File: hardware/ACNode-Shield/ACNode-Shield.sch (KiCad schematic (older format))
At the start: 8 parts

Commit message: PCB rev 1
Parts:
- removed CON?: SD_Card, 10067847-001, symbol SD_Card
- added C1: 10nF, Capacitors_SMD:C_1210_HandSoldering, symbol C_Small
- added D1: 1N4007, Diodes_ThroughHole:Diode_DO-41_SOD81_Horizontal_RM10, symbol D
- added J1: MICRO_SD_HINGE, armory:MICRO_SD_HINGE_AMP, symbol MICRO_SD_HINGE
- added P2: CONN_RELAY, Pin_Headers:Pin_Header_Straight_1x03, symbol CONN_01X03
- added Q1: PN2222A, TO_SOT_Packages_THT:TO-92_Inline_Wide, symbol PN2222A
- added R1: 10k, Resistors_ThroughHole:Resistor_Horizontal_RM10mm, symbol R
- added R2: 100, Resistors_ThroughHole:Resistor_Horizontal_RM10mm, symbol R
- added SW2: SW_BTN, Socket_Strips:Socket_Strip_Straight_1x02, symbol SW_PUSH
- added U1: SRD-05VDC-SL-C, Relays_ThroughHole:Relay_SANYOU_SRD_Series_Form_C, symbol SRD-05VDC-SL-C
- P1, P3: renamed from P?; footprint (none) -> Pin_Headers:Pin_Header_Straight_1x04
- P4, P5: renamed from P?; footprint (none) -> Socket_Strips:Socket_Strip_Straight_2x10
- P6: renamed from P?; footprint (none) -> Pin_Headers:Pin_Header_Straight_1x03
- SW1: renamed from SW?; footprint (none) -> Buttons_Switches_ThroughHole:SW_PUSH_SMALL
- U2: renamed from U?; footprint (none) -> ws2812:WS2812b
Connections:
- net PQ2/PA3 is gone; now on net PQ2: P5.12 (P12)
- net PQ3/PA2 is gone; now on net PQ3: P5.14 (P14)
- net +3.3v: now also C1.2, J1.5 (CLK)
- net +5V: now also D1.1 (K), U1.5 (RL)
- net GND: now also C1.1, J1.3 (CMD), R2.2, SW2.2
- net PB4: no longer U2.4 (DIN)
- net PG1: now also R1.2
- net PM7: now also SW2.1
- net PP5: now also U2.4 (DIN)
- net PQ0: now also J1.4 (VDD)
- net PQ1: now also J1.7 (DAT0)
- net PQ2: now also J1.2 (DAT3/CD)
- net PQ3: now also J1.6 (VSS/GND)
- new net: P2.2 (P2), U1.1 (COM)
- new net: D1.2 (A), Q1.3 (C), U1.2 (RL)
- new net: P2.3 (P3), U1.3 (NC)
- new net: P2.1 (P1), U1.4 (NO)
- new net: Q1.1 (E), R2.1
- new net: Q1.2 (B), R1.1
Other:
- moved on the sheet: P4, P5

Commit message: Removed a resistor, fixed some tracks.
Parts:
- removed R2: 100, Resistors_ThroughHole:Resistor_Horizontal_RM10mm, symbol R
- R1: value 10k -> 1k
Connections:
- net GND: now also Q1.1 (E)
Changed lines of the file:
@@
 +5V
-$Comp
-L R R2
-U 1 1 572DD805
-P 2750 3050
-F 0 "R2" H 2820 3096 50  0000 L CNN
-F 1 "100" H 2820 3004 50  0000 L CNN
-F 2 "Resistors_ThroughHole:Resistor_Horizontal_RM10mm" V 2680 3050 50  0001 C CNN
-F 3 "" H 2750 3050 50  0000 C CNN
-	1    2750 3050
-	1    0    0    -1
-$EndComp
 $Comp
 L D D1
@@
 Connection ~ 2750 1850
 Wire Wire Line
-	2750 2800 2750 2900
+	2750 2800 2750 3300
 Text GLabel 2100 3300 0    60   Input ~ 0
 GND
 Wire Wire Line
-	2100 3300 2750 3300
-Wire Wire Line
-	2750 3300 2750 3200
+	2750 3300 2100 3300
 $Comp
 L R R1
@@
 P 2200 2600
 F 0 "R1" V 1992 2600 50  0000 C CNN
-F 1 "10k" V 2084 2600 50  0000 C CNN
+F 1 "1k" V 2084 2600 50  0000 C CNN
 F 2 "Resistors_ThroughHole:Resistor_Horizontal_RM10mm" V 2130 2600 50  0001 C CNN
 F 3 "" H 2200 2600 50  0000 C CNN

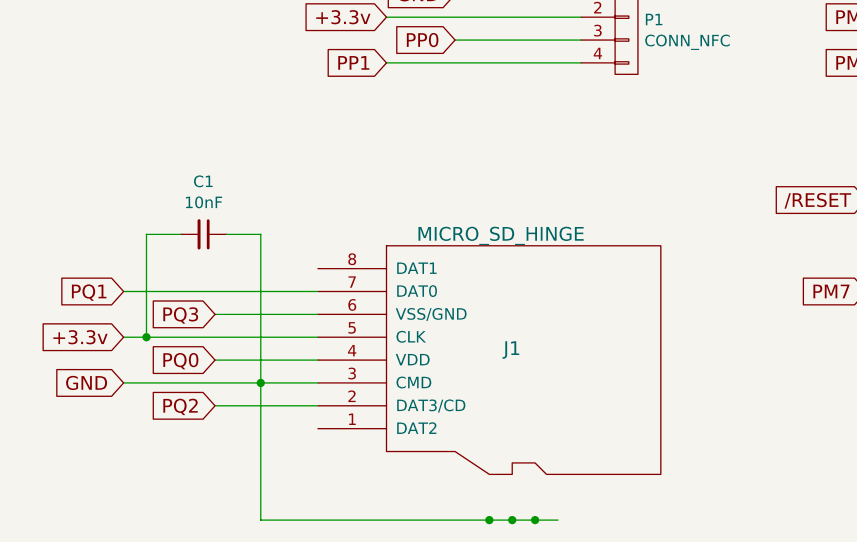
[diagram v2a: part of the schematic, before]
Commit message: Moved components around, changed MicroSD card receptacle footprint (was flipped (!)).
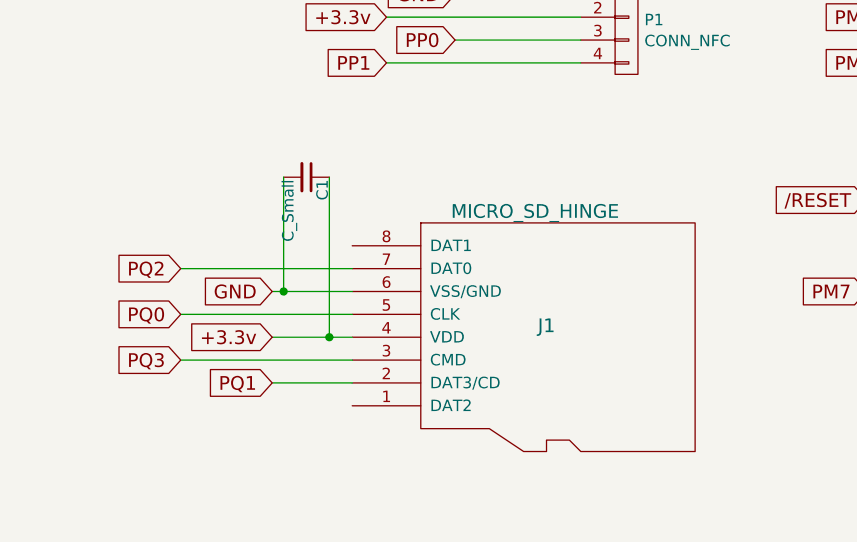
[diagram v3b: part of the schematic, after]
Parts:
- C1: value 10nF -> C_Small; footprint Capacitors_SMD:C_1210_HandSoldering -> Capacitors_SMD:C_1206
- J1: footprint armory:MICRO_SD_HINGE_AMP -> MicroSD:MICRO_SD_HINGE_CHINA
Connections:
- net +3.3v: now also C1.1, J1.4 (VDD); no longer C1.2, J1.5 (CLK)
- net GND: now also C1.2, J1.6 (VSS/GND); no longer C1.1, J1.3 (CMD)
- net PQ0: now also J1.5 (CLK); no longer J1.4 (VDD)
- net PQ1: now also J1.2 (DAT3/CD); no longer J1.7 (DAT0)
- net PQ2: now also J1.7 (DAT0); no longer J1.2 (DAT3/CD)
- net PQ3: now also J1.3 (CMD); no longer J1.6 (VSS/GND)
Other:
- moved on the sheet: J1
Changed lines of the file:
@@
 	9900 5100 9900 4450
 Connection ~ 9900 4450
-Text GLabel 1950 6500 0    60   Input ~ 0
-PQ2
-Text GLabel 1950 6100 0    60   Input ~ 0
-PQ3
-Text GLabel 1550 6200 0    60   Input ~ 0
-+3.3v
-Text GLabel 1550 6400 0    60   Input ~ 0
-GND
-Text GLabel 1950 6300 0    60   Input ~ 0
-PQ0
-Text GLabel 1550 6000 0    60   Input ~ 0
-PQ1
-Wire Wire Line
-	1950 6100 2400 6100
-Wire Wire Line
-	1550 6000 2400 6000
 $Comp
 L SW_PUSH SW2
@@
 	3900 2100 4200 2100
 $Comp
-L C_Small C1
-U 1 1 572DE1F3
-P 1900 5750
-F 0 "C1" V 1670 5750 50  0000 C CNN
-F 1 "10nF" V 1762 5750 50  0000 C CNN
-F 2 "Capacitors_SMD:C_1210_HandSoldering" H 1900 5750 50  0001 C CNN
-F 3 "" H 1900 5750 50  0000 C CNN
-	1    1900 5750
-	0    1    1    0
-$EndComp
-$Comp
 L PN2222A Q1
 U 1 1 572E2FF6
@@
 L MICRO_SD_HINGE J1
 U 1 1 572E391C
-P 3200 6300
-F 0 "J1" H 3250 6350 60  0000 C CNN
-F 1 "MICRO_SD_HINGE" H 3200 6850 60  0000 C CNN
-F 2 "armory:MICRO_SD_HINGE_AMP" V 3310 5800 60  0001 C CNN
-F 3 "" V 3310 5800 60  0000 C CNN
-	1    3200 6300
+P 3350 6200
+F 0 "J1" H 3400 6250 60  0000 C CNN
+F 1 "MICRO_SD_HINGE" H 3350 6750 60  0000 C CNN
+F 2 "MicroSD:MICRO_SD_HINGE_CHINA" V 3460 5700 60  0001 C CNN
+F 3 "" V 3460 5700 60  0000 C CNN
+	1    3350 6200
 	1    0    0    -1
 $EndComp
+Text GLabel 2200 6400 0    60   Input ~ 0
+PQ1
+Text GLabel 1800 6300 0    60   Input ~ 0
+PQ3
+Text GLabel 2200 6200 0    60   Input ~ 0
++3.3v
+Text GLabel 1800 6100 0    60   Input ~ 0
+PQ0
+Text GLabel 2200 6000 0    60   Input ~ 0
+GND
+Text GLabel 1800 5900 0    60   Input ~ 0
+PQ2
 Wire Wire Line
-	1550 6400 2400 6400
+	2200 6400 2550 6400
 Wire Wire Line
-	2400 6500 1950 6500
+	2550 6300 1800 6300
 Wire Wire Line
-	1550 6200 2400 6200
+	2200 6200 2550 6200
 Wire Wire Line
-	1950 6300 2400 6300
+	1800 6100 2550 6100
 Wire Wire Line
-	1800 5750 1650 5750
+	2550 6000 2200 6000
 Wire Wire Line
-	1650 5750 1650 6200
-Connection ~ 1650 6200
+	1800 5900 2550 5900
+$Comp
+L C_Small C1
+U 1 1 5736F818
+P 2350 5500
+F 0 "C1" H 2360 5570 50  0000 L CNN
+F 1 "C_Small" H 2360 5420 50  0000 L CNN
+F 2 "Capacitors_SMD:C_1206" H 2350 5500 50  0001 C CNN
+F 3 "" H 2350 5500 50  0000 C CNN
+	1    2350 5500
+	0    1    1    0
+$EndComp
 Wire Wire Line
-	2000 5750 2150 5750
+	2250 5500 2250 6000
+Connection ~ 2250 6000
 Wire Wire Line
-	2150 5750 2150 7000
-Connection ~ 2150 6400
-Wire Wire Line
-	2150 7000 3450 7000
-Connection ~ 3350 7000
-Connection ~ 3250 7000
-Connection ~ 3150 7000
+	2450 5500 2450 6200
+Connection ~ 2450 6200
 $EndSCHEMATC

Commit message: Updated the MicroSD slot component, based on precise drawings.
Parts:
- J1: footprint MicroSD:MICRO_SD_HINGE_CHINA -> SD_Slots:MicroSD_Slot
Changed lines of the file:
@@
 F 0 "J1" H 3400 6250 60  0000 C CNN
 F 1 "MICRO_SD_HINGE" H 3350 6750 60  0000 C CNN
-F 2 "MicroSD:MICRO_SD_HINGE_CHINA" V 3460 5700 60  0001 C CNN
+F 2 "SD_Slots:MicroSD_Slot" V 3460 5700 60  0001 C CNN
 F 3 "" V 3460 5700 60  0000 C CNN
 	1    3350 6200

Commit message: Rev 2 off to the fab
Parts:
- added CON1: SD_Card, SD_Slots:SD_Slot, symbol SD_Card
- P2: footprint Pin_Headers:Pin_Header_Straight_1x03 -> Terminal_Blocks:TerminalBlock_Pheonix_MKDS1.5-3pol
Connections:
- net +3.3v: now also CON1.4 (VDD)
- net GND: now also CON1.6 (VSS)
- net PQ0: now also CON1.5 (CLK)
- net PQ1: now also CON1.1 (CD/DAT3)
- net PQ2: now also CON1.7 (DAT0)
- net PQ3: now also CON1.2 (CMD)
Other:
- moved on the sheet: C1, J1, P1, P3, SW1, SW2
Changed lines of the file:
@@
 L CONN_01X04 P1
 U 1 1 572DBA37
-P 3750 4850
-F 0 "P1" H 3828 4888 50  0000 L CNN
-F 1 "CONN_NFC" H 3828 4796 50  0000 L CNN
-F 2 "Pin_Headers:Pin_Header_Straight_1x04" H 3750 4850 50  0001 C CNN
-F 3 "" H 3750 4850 50  0000 C CNN
-	1    3750 4850
-	1    0    0    -1
-$EndComp
-Text GLabel 3000 4700 0    60   Input ~ 0
-GND
-Text GLabel 2700 4800 0    60   Input ~ 0
+P 3600 4250
+F 0 "P1" H 3678 4288 50  0000 L CNN
+F 1 "CONN_NFC" H 3678 4196 50  0000 L CNN
+F 2 "Pin_Headers:Pin_Header_Straight_1x04" H 3600 4250 50  0001 C CNN
+F 3 "" H 3600 4250 50  0000 C CNN
+	1    3600 4250
+	1    0    0    -1
+$EndComp
+Text GLabel 2850 4100 0    60   Input ~ 0
+GND
+Text GLabel 2550 4200 0    60   Input ~ 0
 +3.3v
-Text GLabel 3000 4900 0    60   Input ~ 0
+Text GLabel 2850 4300 0    60   Input ~ 0
 PP0
-Text GLabel 2700 5000 0    60   Input ~ 0
+Text GLabel 2550 4400 0    60   Input ~ 0
 PP1
 Wire Wire Line
-	3000 4700 3550 4700
-Wire Wire Line
-	3550 4800 2700 4800
-Wire Wire Line
-	3000 4900 3550 4900
-Wire Wire Line
-	3550 5000 2700 5000
+	2850 4100 3400 4100
+Wire Wire Line
+	3400 4200 2550 4200
+Wire Wire Line
+	2850 4300 3400 4300
+Wire Wire Line
+	3400 4400 2550 4400
 $Comp
 L CONN_01X04 P3
 U 1 1 572DBB8D
-P 5950 4850
-F 0 "P3" H 6028 4888 50  0000 L CNN
-F 1 "CONN_RGB_LED" H 6028 4796 50  0000 L CNN
-F 2 "Pin_Headers:Pin_Header_Straight_1x04" H 5950 4850 50  0001 C CNN
-F 3 "" H 5950 4850 50  0000 C CNN
-	1    5950 4850
-	1    0    0    -1
-$EndComp
-Text GLabel 5300 4700 0    60   Input ~ 0
+P 5800 4250
+F 0 "P3" H 5878 4288 50  0000 L CNN
+F 1 "CONN_RGB_LED" H 5878 4196 50  0000 L CNN
+F 2 "Pin_Headers:Pin_Header_Straight_1x04" H 5800 4250 50  0001 C CNN
+F 3 "" H 5800 4250 50  0000 C CNN
+	1    5800 4250
+	1    0    0    -1
+$EndComp
+Text GLabel 5150 4100 0    60   Input ~ 0
 +3.3v
-Text GLabel 4900 4800 0    60   Input ~ 0
+Text GLabel 4750 4200 0    60   Input ~ 0
 PM0
-Text GLabel 5300 4900 0    60   Input ~ 0
+Text GLabel 5150 4300 0    60   Input ~ 0
 PM1
-Text GLabel 4900 5000 0    60   Input ~ 0
+Text GLabel 4750 4400 0    60   Input ~ 0
 PM2
 Wire Wire Line
-	5300 4700 5750 4700
-Wire Wire Line
-	5750 4800 4900 4800
-Wire Wire Line
-	5300 4900 5750 4900
-Wire Wire Line
-	5750 5000 4900 5000
+	5150 4100 5600 4100
+Wire Wire Line
+	5600 4200 4750 4200
+Wire Wire Line
+	5150 4300 5600 4300
+Wire Wire Line
+	5600 4400 4750 4400
 $Comp
 L SW_PUSH SW1
 U 1 1 572DBD3B
-P 5350 5600
-F 0 "SW1" H 5350 5856 50  0000 C CNN
-F 1 "SW_RST" H 5350 5764 50  0000 C CNN
-F 2 "Buttons_Switches_ThroughHole:SW_PUSH_SMALL" H 5350 5600 50  0001 C CNN
-F 3 "" H 5350 5600 50  0000 C CNN
-	1    5350 5600
-	1    0    0    -1
-$EndComp
-Text GLabel 4800 5600 0    60   Input ~ 0
+P 9150 5550
+F 0 "SW1" H 9150 5806 50  0000 C CNN
+F 1 "SW_RST" H 9150 5714 50  0000 C CNN
+F 2 "Buttons_Switches_ThroughHole:SW_PUSH_SMALL" H 9150 5550 50  0001 C CNN
+F 3 "" H 9150 5550 50  0000 C CNN
+	1    9150 5550
+	1    0    0    -1
+$EndComp
+Text GLabel 8600 5550 0    60   Input ~ 0
 /RESET
-Text GLabel 5900 5600 2    60   Input ~ 0
-GND
-Wire Wire Line
-	5650 5600 5900 5600
-Wire Wire Line
-	5050 5600 4800 5600
+Text GLabel 9700 5550 2    60   Input ~ 0
+GND
+Wire Wire Line
+	9450 5550 9700 5550
+Wire Wire Line
+	8850 5550 8600 5550
 $Comp
 L WS2812B U2
@@
 L SW_PUSH SW2
 U 1 1 572DC67E
-P 5350 6000
-F 0 "SW2" H 5350 6256 50  0000 C CNN
-F 1 "SW_BTN" H 5350 6164 50  0000 C CNN
-F 2 "Socket_Strips:Socket_Strip_Straight_1x02" H 5350 6000 50  0001 C CNN
-F 3 "" H 5350 6000 50  0000 C CNN
-	1    5350 6000
-	1    0    0    -1
-$EndComp
-Text GLabel 5900 6000 2    60   Input ~ 0
-GND
-Text GLabel 4800 6000 0    60   Input ~ 0
+P 9150 5950
+F 0 "SW2" H 9150 6206 50  0000 C CNN
+F 1 "SW_BTN" H 9150 6114 50  0000 C CNN
+F 2 "Socket_Strips:Socket_Strip_Straight_1x02" H 9150 5950 50  0001 C CNN
+F 3 "" H 9150 5950 50  0000 C CNN
+	1    9150 5950
+	1    0    0    -1
+$EndComp
+Text GLabel 9700 5950 2    60   Input ~ 0
+GND
+Text GLabel 8600 5950 0    60   Input ~ 0
 PM7
 Wire Wire Line
-	4800 6000 5050 6000
-Wire Wire Line
-	5650 6000 5900 6000
+	8600 5950 8850 5950
+Wire Wire Line
+	9450 5950 9700 5950
 $Comp
 L SRD-05VDC-SL-C U1
@@
 F 0 "P2" H 4478 2038 50  0000 L CNN
 F 1 "CONN_RELAY" H 4478 1946 50  0000 L CNN
-F 2 "Pin_Headers:Pin_Header_Straight_1x03" H 4400 2000 50  0001 C CNN
+F 2 "Terminal_Blocks:TerminalBlock_Pheonix_MKDS1.5-3pol" H 4400 2000 50  0001 C CNN
 F 3 "" H 4400 2000 50  0000 C CNN
 	1    4400 2000
@@
 L MICRO_SD_HINGE J1
 U 1 1 572E391C
-P 3350 6200
-F 0 "J1" H 3400 6250 60  0000 C CNN
-F 1 "MICRO_SD_HINGE" H 3350 6750 60  0000 C CNN
-F 2 "SD_Slots:MicroSD_Slot" V 3460 5700 60  0001 C CNN
-F 3 "" V 3460 5700 60  0000 C CNN
-	1    3350 6200
-	1    0    0    -1
-$EndComp
-Text GLabel 2200 6400 0    60   Input ~ 0
+P 5150 5400
+F 0 "J1" H 5200 5450 60  0000 C CNN
+F 1 "MICRO_SD_HINGE" H 5150 5950 60  0000 C CNN
+F 2 "SD_Slots:MicroSD_Slot" V 5260 4900 60  0001 C CNN
+F 3 "" V 5260 4900 60  0000 C CNN
+	1    5150 5400
+	1    0    0    -1
+$EndComp
+Text GLabel 2350 5600 0    60   Input ~ 0
 PQ1
-Text GLabel 1800 6300 0    60   Input ~ 0
+Text GLabel 1950 5500 0    60   Input ~ 0
 PQ3
-Text GLabel 2200 6200 0    60   Input ~ 0
+Text GLabel 2350 5400 0    60   Input ~ 0
 +3.3v
-Text GLabel 1800 6100 0    60   Input ~ 0
+Text GLabel 1950 5300 0    60   Input ~ 0
 PQ0
-Text GLabel 2200 6000 0    60   Input ~ 0
-GND
-Text GLabel 1800 5900 0    60   Input ~ 0
+Text GLabel 2350 5200 0    60   Input ~ 0
+GND
+Text GLabel 1950 5100 0    60   Input ~ 0
 PQ2
 Wire Wire Line
-	2200 6400 2550 6400
-Wire Wire Line
-	2550 6300 1800 6300
-Wire Wire Line
-	2200 6200 2550 6200
-Wire Wire Line
-	1800 6100 2550 6100
-Wire Wire Line
-	2550 6000 2200 6000
-Wire Wire Line
-	1800 5900 2550 5900
+	2350 5600 4350 5600
+Wire Wire Line
+	1950 5500 4350 5500
+Wire Wire Line
+	2350 5400 4350 5400
+Wire Wire Line
+	1950 5300 4350 5300
+Wire Wire Line
+	2350 5200 4350 5200
+Wire Wire Line
+	1950 5100 4350 5100
 $Comp
 L C_Small C1
 U 1 1 5736F818
-P 2350 5500
-F 0 "C1" H 2360 5570 50  0000 L CNN
-F 1 "C_Small" H 2360 5420 50  0000 L CNN
-F 2 "Capacitors_SMD:C_1206" H 2350 5500 50  0001 C CNN
-F 3 "" H 2350 5500 50  0000 C CNN
-	1    2350 5500
+P 2500 4700
+F 0 "C1" H 2510 4770 50  0000 L CNN
+F 1 "C_Small" H 2510 4620 50  0000 L CNN
+F 2 "Capacitors_SMD:C_1206" H 2500 4700 50  0001 C CNN
+F 3 "" H 2500 4700 50  0000 C CNN
+	1    2500 4700
 	0    1    1    0
 $EndComp
 Wire Wire Line
-	2250 5500 2250 6000
-Connection ~ 2250 6000
-Wire Wire Line
-	2450 5500 2450 6200
-Connection ~ 2450 6200
+	2400 4700 2400 5200
+Connection ~ 2400 5200
+Wire Wire Line
+	2600 4700 2600 5400
+Connection ~ 2600 5400
+$Comp
+L SD_Card CON1
+U 1 1 57ED844B
+P 5050 6800
+F 0 "CON1" H 4400 7350 50  0000 C CNN
+F 1 "SD_Card" H 5650 6250 50  0000 C CNN
+F 2 "SD_Slots:SD_Slot" H 5250 7150 50  0000 C CNN
+F 3 "" H 5050 6800 50  0000 C CNN
+	1    5050 6800
+	1    0    0    -1
+$EndComp
+Wire Wire Line
+	4150 7100 4050 7100
+Wire Wire Line
+	4050 7100 4050 5100
+Connection ~ 4050 5100
+Wire Wire Line
+	4150 7000 3950 7000
+Wire Wire Line
+	3950 7000 3950 5200
+Connection ~ 3950 5200
+Wire Wire Line
+	4150 6900 3850 6900
+Wire Wire Line
+	3850 6900 3850 5300
+Connection ~ 3850 5300
+Wire Wire Line
+	4150 6800 3750 6800
+Wire Wire Line
+	3750 6800 3750 5400
+Connection ~ 3750 5400
+Wire Wire Line
+	4150 6600 3650 6600
+Wire Wire Line
+	3650 6600 3650 5500
+Connection ~ 3650 5500
+Wire Wire Line
+	4150 6500 3550 6500
+Wire Wire Line
+	3550 6500 3550 5600
+Connection ~ 3550 5600
 $EndSCHEMATC

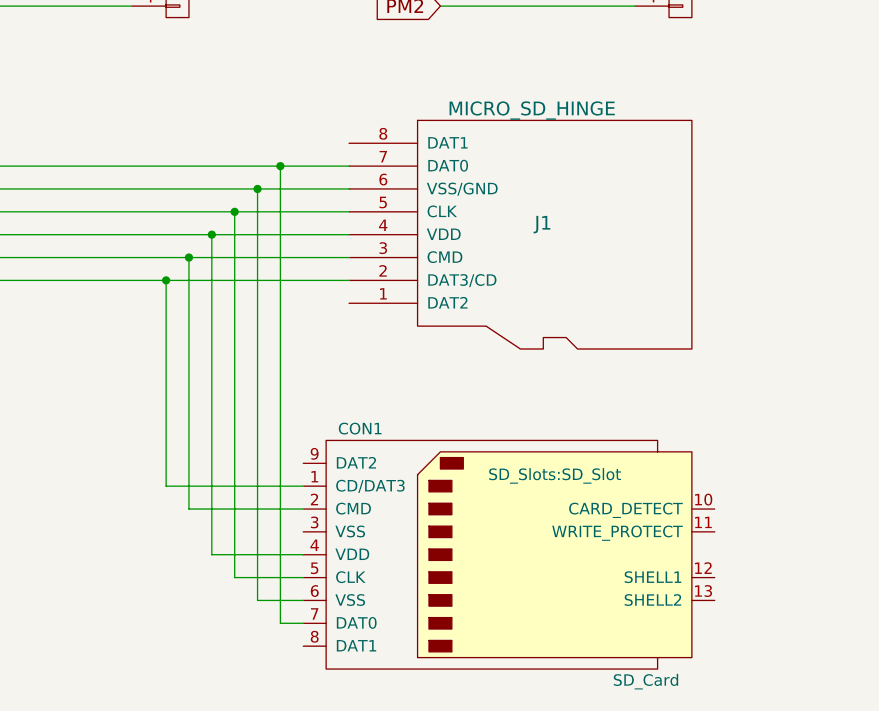
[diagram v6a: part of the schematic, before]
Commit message: Removed large SD card connector - it doesn't fit.
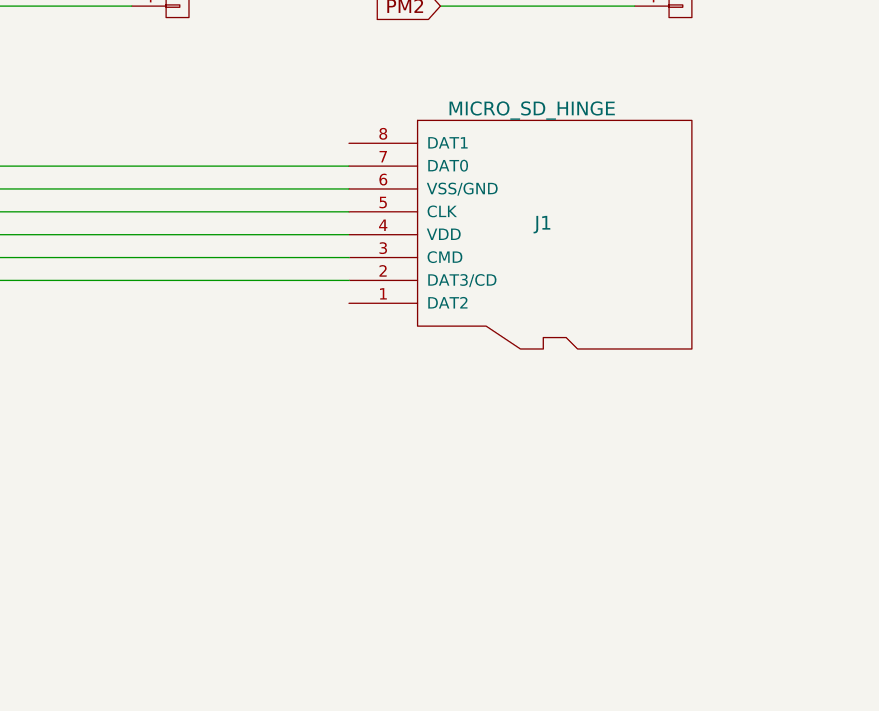
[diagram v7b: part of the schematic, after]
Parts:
- removed CON1: SD_Card, SD_Slots:SD_Slot, symbol SD_Card
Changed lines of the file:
@@
 	2600 4700 2600 5400
 Connection ~ 2600 5400
-$Comp
-L SD_Card CON1
-U 1 1 57ED844B
-P 5050 6800
-F 0 "CON1" H 4400 7350 50  0000 C CNN
-F 1 "SD_Card" H 5650 6250 50  0000 C CNN
-F 2 "SD_Slots:SD_Slot" H 5250 7150 50  0000 C CNN
-F 3 "" H 5050 6800 50  0000 C CNN
-	1    5050 6800
-	1    0    0    -1
-$EndComp
-Wire Wire Line
-	4150 7100 4050 7100
-Wire Wire Line
-	4050 7100 4050 5100
-Connection ~ 4050 5100
-Wire Wire Line
-	4150 7000 3950 7000
-Wire Wire Line
-	3950 7000 3950 5200
-Connection ~ 3950 5200
-Wire Wire Line
-	4150 6900 3850 6900
-Wire Wire Line
-	3850 6900 3850 5300
-Connection ~ 3850 5300
-Wire Wire Line
-	4150 6800 3750 6800
-Wire Wire Line
-	3750 6800 3750 5400
-Connection ~ 3750 5400
-Wire Wire Line
-	4150 6600 3650 6600
-Wire Wire Line
-	3650 6600 3650 5500
-Connection ~ 3650 5500
-Wire Wire Line
-	4150 6500 3550 6500
-Wire Wire Line
-	3550 6500 3550 5600
-Connection ~ 3550 5600
 $EndSCHEMATC

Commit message: Reversed contacts on the SD card connector - it should work now.
Bumped revision of the board to 4.
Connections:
- net PQ2: now also J1.3 (CMD); no longer J1.7 (DAT0)
- net PQ3: now also J1.7 (DAT0); no longer J1.3 (CMD)
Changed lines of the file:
@@
 Text GLabel 2350 5600 0    60   Input ~ 0
 PQ1
-Text GLabel 1950 5500 0    60   Input ~ 0
+Text GLabel 1950 5100 0    60   Input ~ 0
 PQ3
 Text GLabel 2350 5400 0    60   Input ~ 0
@@
 Text GLabel 2350 5200 0    60   Input ~ 0
 GND
-Text GLabel 1950 5100 0    60   Input ~ 0
+Text GLabel 1950 5500 0    60   Input ~ 0
 PQ2
-Wire Wire Line
-	2350 5600 4350 5600
-Wire Wire Line
-	1950 5500 4350 5500
 Wire Wire Line
 	2350 5400 4350 5400
 Wire Wire Line
-	1950 5300 4350 5300
-Wire Wire Line
 	2350 5200 4350 5200
-Wire Wire Line
-	1950 5100 4350 5100
 $Comp
 L C_Small C1
@@
 	2600 4700 2600 5400
 Connection ~ 2600 5400
+Wire Wire Line
+	2350 5600 4350 5600
+Wire Wire Line
+	1950 5300 4350 5300
+Wire Wire Line
+	1950 5500 4350 5500
+Wire Wire Line
+	1950 5100 4350 5100
 $EndSCHEMATC
